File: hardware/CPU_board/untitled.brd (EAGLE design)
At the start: 128.9 x 94.9 mm, 60 parts, among them IC1 MAX232ECWE, IC2 MAX232ECWE, IC3 AM29F040J, IC4 74HCT138D, IC5 LM2596S, J2 POWER_JACKSLT, U1 AS6C4008-55SIN, Y1 CRYSTAL-GROUNDEDSMD-5X3.2

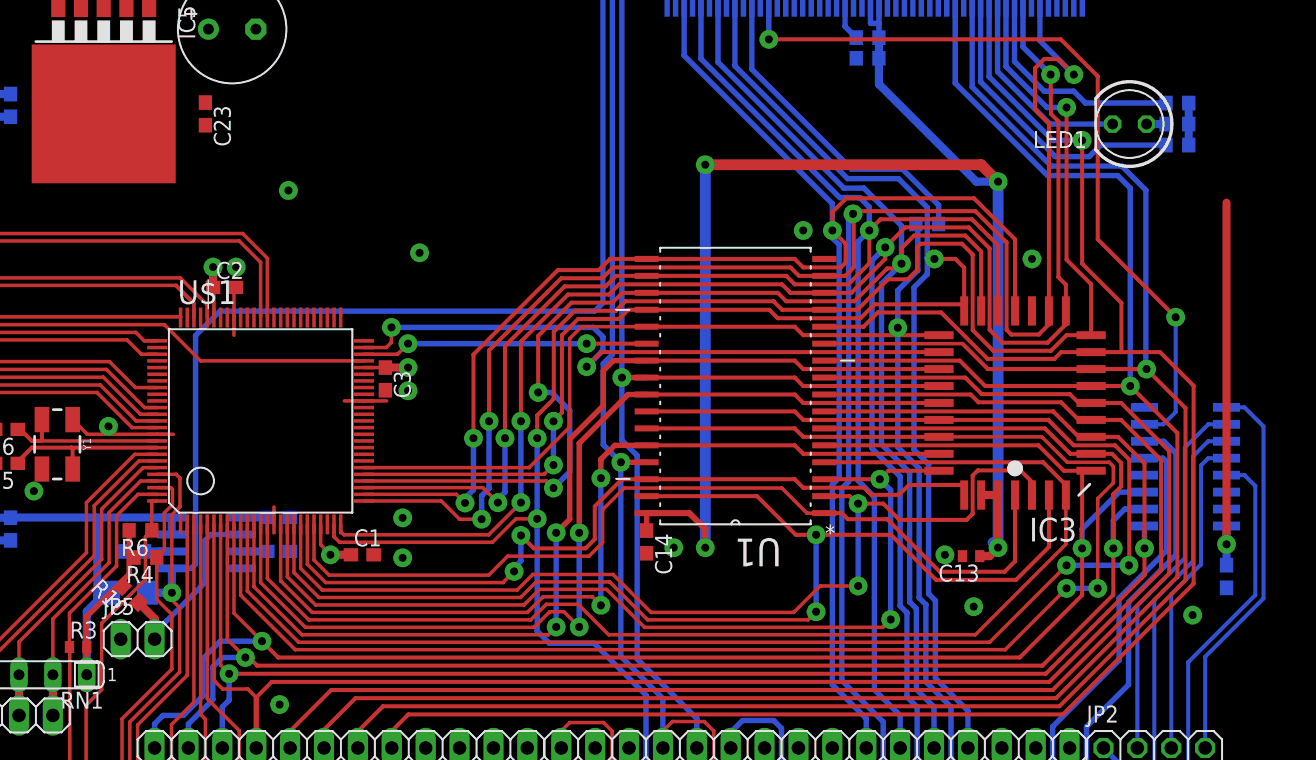
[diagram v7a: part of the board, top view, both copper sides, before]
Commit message: Connector instead LED on board
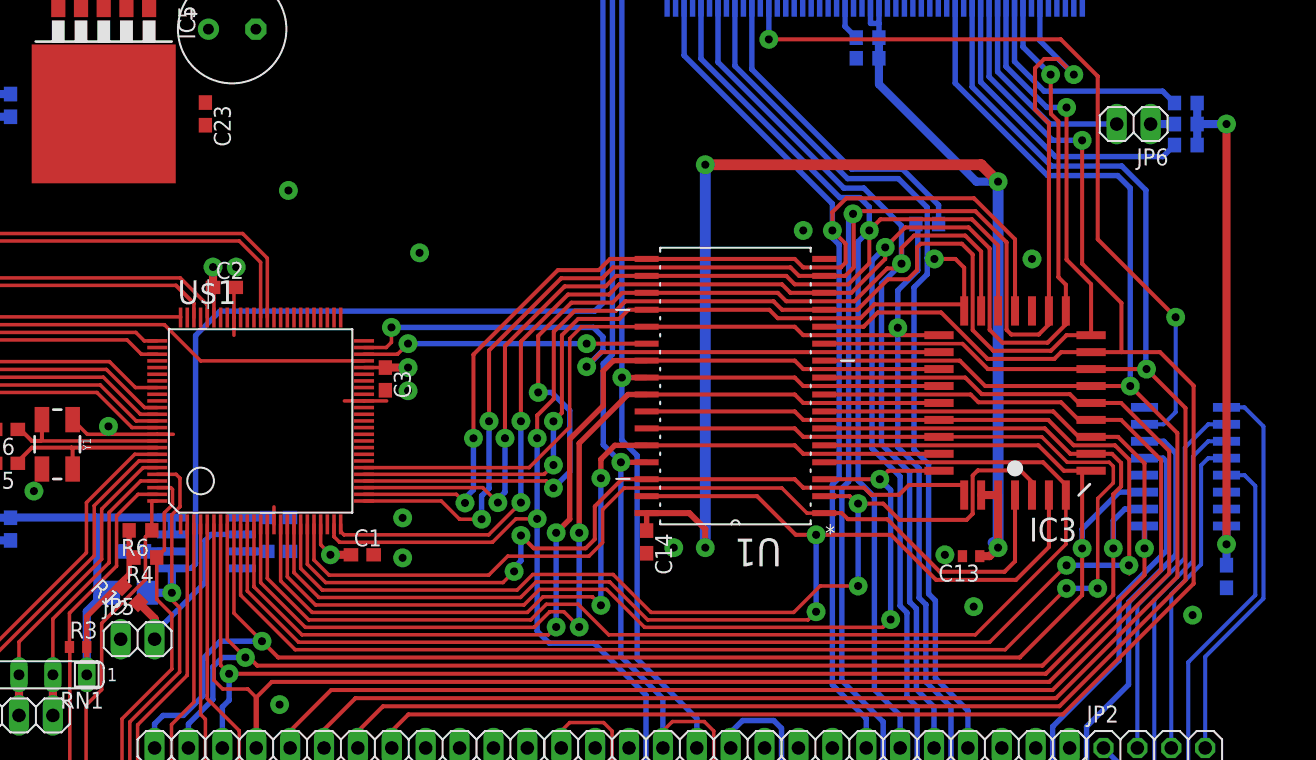
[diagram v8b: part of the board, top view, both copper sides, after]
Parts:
- removed LED1: (no value), led:LED5MM
- added JP6: (no value), pinhead:1X02
- moved R1 0.64 mm to (114.1, 57.3)
- moved R13 0.64 mm to (114.1, 55.8)
- moved R8 0.64 mm to (114.1, 54.2)
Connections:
- net N$32: now also JP6.1; no longer LED1.A
- net N$33: now also JP6.2; no longer LED1.K
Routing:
- net 5V: track 214.3 -> 222.5 mm
- net N$30: track 17.9 -> 18.5 mm
- net N$27: track 23.3 -> 24.0 mm
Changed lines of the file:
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@@
 </element>
 <element name="R7" library="rcl" package="R0603" value="" x="90.2716" y="62.23" rot="MR180"/>
-<element name="R8" library="rcl" package="R0603" value="" x="113.4872" y="54.1782" rot="MR180"/>
-<element name="R1" library="rcl" package="R0603" value="" x="113.4872" y="57.3278" rot="MR180"/>
+<element name="R8" library="rcl" package="R0603" value="" x="114.1222" y="54.1782" rot="MR180"/>
+<element name="R1" library="rcl" package="R0603" value="" x="114.1222" y="57.3278" rot="MR180"/>
 <element name="R12" library="rcl" package="R0603" value="" x="90.2716" y="60.6806" rot="MR180"/>
-<element name="R13" library="rcl" package="R0603" value="" x="113.4872" y="55.753" rot="MR180"/>
-<element name="LED1" library="led" package="LED5MM" value="" x="109.9058" y="55.753" rot="R180"/>
+<element name="R13" library="rcl" package="R0603" value="" x="114.1222" y="55.753" rot="MR180"/>
 <element name="R2" library="rcl" package="R0603" value="" x="94.742" y="48.26" rot="MR0"/>
 <element name="IC4" library="74xx-eu" package="SO16" value="74HCT138D" x="114.0968" y="30.0736" rot="MR90"/>
@@
 <element name="JP5" library="pinhead" package="1X02" value="" x="35.56" y="17.145"/>
 <element name="R10" library="rcl" package="R0603" value="" x="35.0266" y="20.4978" rot="R135"/>
+<element name="JP6" library="pinhead" package="1X02" value="" x="110.2106" y="55.753" rot="R180"/>
 </elements>
 <signals>
@@
 <wire x1="117.1702" y1="24.257" x2="117.1702" y2="25.6286" width="0.6096" layer="16"/>
 <wire x1="117.1702" y1="24.257" x2="117.1702" y2="22.694" width="0.6096" layer="16"/>
-<wire x1="117.1702" y1="24.257" x2="117.1702" y2="49.8602" width="0.6096" layer="1"/>
+<wire x1="117.1702" y1="24.257" x2="117.1702" y2="55.753" width="0.6096" layer="1"/>
 <contactref element="R4" pad="2"/>
 <contactref element="R5" pad="2"/>
@@
 <wire x1="91.1216" y1="58.7384" x2="98.425" y2="51.435" width="0.6096" layer="16"/>
 <wire x1="100.0506" y1="51.435" x2="98.425" y2="51.435" width="0.6096" layer="16"/>
-<wire x1="114.3372" y1="54.1782" x2="114.3372" y2="55.753" width="0.6096" layer="16"/>
-<wire x1="114.3372" y1="55.753" x2="114.3372" y2="57.3278" width="0.6096" layer="16"/>
+<wire x1="114.9722" y1="54.1782" x2="114.9722" y2="55.753" width="0.6096" layer="16"/>
+<wire x1="114.9722" y1="55.753" x2="114.9722" y2="57.3278" width="0.6096" layer="16"/>
 <contactref element="RN1" pad="1"/>
 <contactref element="R3" pad="2"/>
-<wire x1="31.75" y1="14.478" x2="31.75" y2="14.605" width="0.4064" layer="1"/>
 <contactref element="R6" pad="2"/>
-<wire x1="31.75" y1="14.605" x2="31.75" y2="16.51" width="0.4064" layer="1"/>
+<wire x1="31.75" y1="14.478" x2="31.75" y2="16.51" width="0.4064" layer="1"/>
 <wire x1="31.75" y1="16.51" x2="31.75" y2="18.8468" width="0.4064" layer="1"/>
 <wire x1="31.7523" y1="16.5608" x2="31.7523" y2="16.5123" width="0.2667" layer="1"/>
@@
 <wire x1="26.0486" y1="26.2636" x2="26.035" y2="26.25" width="0.6096" layer="16"/>
 <wire x1="38.1162" y1="24.9936" x2="38.1162" y2="26.2636" width="0.6096" layer="16"/>
-<via x="31.75" y="14.605" extent="1-16" drill="0.6" shape="square"/>
 <wire x1="31.75" y1="14.605" x2="31.75" y2="19.2278" width="0.6096" layer="16"/>
 <wire x1="34.9259" y1="25.2984" x2="34.9259" y2="23.495" width="0.4064" layer="1"/>
@@
 <wire x1="34.42555625" y1="21.098840625" x2="34.146159375" y2="21.098840625" width="0.2667" layer="1"/>
 <wire x1="34.146159375" y1="21.098840625" x2="34.0741" y2="21.1709" width="0.2667" layer="1"/>
-<wire x1="117.1702" y1="49.8602" x2="114.3372" y2="54.1782" width="0" layer="19" extent="1-16"/>
-<wire x1="100.0506" y1="51.435" x2="114.3372" y2="54.1782" width="0" layer="19" extent="16-16"/>
+<wire x1="31.75" y1="14.478" x2="31.75" y2="14.605" width="0.4064" layer="16"/>
+<via x="117.1702" y="55.753" extent="1-16" drill="0.6" diameter="1.4224" shape="octagon"/>
+<wire x1="114.9722" y1="55.753" x2="117.1702" y2="55.753" width="0.6096" layer="16"/>
+<wire x1="100.0506" y1="51.435" x2="114.9722" y2="54.1782" width="0" layer="19" extent="16-16"/>
 <wire x1="55.8292" y1="37.5026" x2="73.7108" y2="26.5938" width="0" layer="19" extent="1-1"/>
 <wire x1="41.2802" y1="41.2526" x2="52.5302" y2="37.5026" width="0" layer="19" extent="1-1"/>
@@
 <wire x1="98.7425" y1="65.675" x2="98.7425" y2="58.9153" width="0.4064" layer="16"/>
 <wire x1="98.7425" y1="58.9153" x2="104.3432" y2="53.3146" width="0.4064" layer="16"/>
-<wire x1="112.6372" y1="54.1782" x2="107.7468" y2="54.1782" width="0.4064" layer="16"/>
-<wire x1="107.7468" y1="54.1782" x2="106.8832" y2="53.3146" width="0.4064" layer="16"/>
-<wire x1="104.3432" y1="53.3146" x2="106.8832" y2="53.3146" width="0.4064" layer="16"/>
+<wire x1="104.3432" y1="53.3146" x2="112.4086" y2="53.3146" width="0.4064" layer="16"/>
+<wire x1="112.4086" y1="53.3146" x2="113.2722" y2="54.1782" width="0.4064" layer="16"/>
 </signal>
 <signal name="N$29">
@@
 <wire x1="101.2825" y1="65.675" x2="101.2825" y2="60.4393" width="0.4064" layer="16"/>
 <wire x1="101.2825" y1="60.4393" x2="103.505" y2="58.2168" width="0.4064" layer="16"/>
-<wire x1="103.505" y1="58.2168" x2="105.7148" y2="58.2168" width="0.4064" layer="16"/>
-<wire x1="112.6372" y1="57.3278" x2="106.6038" y2="57.3278" width="0.4064" layer="16"/>
-<wire x1="106.6038" y1="57.3278" x2="105.7148" y2="58.2168" width="0.4064" layer="16"/>
+<wire x1="103.505" y1="58.2168" x2="112.3832" y2="58.2168" width="0.4064" layer="16"/>
+<wire x1="112.3832" y1="58.2168" x2="113.2722" y2="57.3278" width="0.4064" layer="16"/>
 </signal>
 <signal name="CF_CS0">
@@
 <signal name="N$32">
 <contactref element="R13" pad="1"/>
-<contactref element="LED1" pad="A"/>
-<wire x1="111.1758" y1="55.753" x2="112.6372" y2="55.753" width="0.6096" layer="16"/>
+<contactref element="JP6" pad="1"/>
+<wire x1="111.4806" y1="55.753" x2="113.2722" y2="55.753" width="0.6096" layer="16"/>
 </signal>
 <signal name="N$33">
 <contactref element="CON1" pad="45"/>
-<contactref element="LED1" pad="K"/>
 <wire x1="100.0125" y1="65.675" x2="100.0125" y2="59.6773" width="0.4064" layer="16"/>
 <wire x1="100.0125" y1="59.6773" x2="103.9368" y2="55.753" width="0.4064" layer="16"/>
-<wire x1="108.6358" y1="55.753" x2="103.9368" y2="55.753" width="0.4064" layer="16"/>
+<contactref element="JP6" pad="2"/>
+<wire x1="103.9368" y1="55.753" x2="108.9406" y2="55.753" width="0.4064" layer="16"/>
 </signal>
 <signal name="N$34">
